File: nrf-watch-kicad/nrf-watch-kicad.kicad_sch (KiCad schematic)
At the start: 78 parts, among them IC1 TLV840MAPL36DBVRQ1, IC2 XC9265C181MR-G, IC3 TPS61023DRLT, IC4 MAX30101EFD+T, M1 Vibrator DC Motor, Q1 DMP2045U-7, Q2 SS8050-G, U1 MAX1811ESA+, U2 DMC2400UV-7, U3 LIS2DS12TR, U4 MX25R6435FZNIL0, U5 u-blox ANNA-B402, U6 DRV2603RUNT, U7 XC9265A331MR-G, U8 TXB0104QRUTRQ1, U9 GC9A01

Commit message: Before moving bottom to top
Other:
- note added: "In case of issues in battery and power management circuit there is a solder bridge that can be unconnected in order for rest of board to still function. If not working I can inject 5V at V_BAT testpoint and at 1.8V regulator CE."
- note added: "Pull-up/down resistors"
- note added: "The 3V3 regulator CE signal will be used as thedisplay reset/on off as nothing else is using 3V3 and I save one level shift for the display RESET signal."
- note removed: "In case of issues in battery and power management circuit there are a solder bridge that can be unconnected in order for rest of board to still function. If not working we can inject 5V at V_BAT testpoint and at 1.8V regulator CE."
- note removed: "Pull-up resistors"
- company: Jakob Krantz -> (none)
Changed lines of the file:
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@@
 (kicad_sch (version 20211123) (generator eeschema)
-  (paper "A2")
+  (paper "User" 419.989 340.004)
   (title_block
     (title "Smart Watch")
     (date "2022-09-05")
     (rev "0.1")
-    (company "Jakob Krantz")
   )
   (junction (at 261.62 55.88) (diameter 0) (color 0 0 0 0)
@@
     (stroke (width 0) (type default) (color 0 0 0 0))
   )
-  (polyline (pts (xy 96.52 152.4) (xy 15.24 152.4))
+  (polyline (pts (xy 73.66 152.4) (xy 15.24 152.4))
     (stroke (width 0) (type default) (color 0 0 0 0))
   )
@@
     (stroke (width 0) (type default) (color 0 0 0 0))
   )
-  (polyline (pts (xy 269.24 281.94) (xy 269.24 121.92))
+  (polyline (pts (xy 271.78 292.1) (xy 269.24 121.92))
     (stroke (width 0) (type default) (color 0 0 0 0))
   )
@@
     (stroke (width 0) (type default) (color 0 0 0 0))
   )
-  (polyline (pts (xy 96.52 121.92) (xy 96.52 152.4))
+  (polyline (pts (xy 73.66 121.92) (xy 73.66 152.4))
     (stroke (width 0) (type default) (color 0 0 0 0))
   )
@@
     (stroke (width 0) (type default) (color 0 0 0 0))
   )
-  (wire (pts (xy 63.5 134.62) (xy 63.5 142.24))
+  (wire (pts (xy 50.8 134.62) (xy 50.8 142.24))
     (stroke (width 0) (type default) (color 0 0 0 0))
   )
@@
     (stroke (width 0) (type default) (color 0 0 0 0))
   )
-  (polyline (pts (xy 172.72 121.92) (xy 172.72 281.94))
+  (polyline (pts (xy 172.72 121.92) (xy 175.26 292.1))
     (stroke (width 0) (type default) (color 0 0 0 0))
   )
@@
     (stroke (width 0) (type default) (color 0 0 0 0))
   )
-  (polyline (pts (xy 172.72 281.94) (xy 269.24 281.94))
+  (polyline (pts (xy 175.26 292.1) (xy 271.78 292.1))
     (stroke (width 0) (type default) (color 0 0 0 0))
   )
@@
     (stroke (width 0) (type default) (color 0 0 0 0))
   )
-  (wire (pts (xy 76.2 134.62) (xy 76.2 139.7))
+  (wire (pts (xy 63.5 134.62) (xy 63.5 139.7))
     (stroke (width 0) (type default) (color 0 0 0 0))
   )
@@
     (stroke (width 0) (type default) (color 0 0 0 0))
   )
-  (polyline (pts (xy 15.24 121.92) (xy 96.52 121.92))
+  (polyline (pts (xy 15.24 121.92) (xy 73.66 121.92))
     (stroke (width 0) (type default) (color 0 0 0 0))
   )
@@
     (effects (font (size 1.27 1.27)) (justify left bottom))
   )
-  (text "Pull-up resistors" (at 109.22 127 0)
+  (text "Pull-up/down resistors" (at 109.22 127 0)
     (effects (font (size 3 3)) (justify left bottom))
   )
@@
     (effects (font (size 1.27 1.27)) (justify left bottom))
   )
-  (text "In case of issues in battery and power management circuit \nthere are a solder bridge that can be unconnected\nin order for rest of board to still function.\n\nIf not working we can inject 5V at V_BAT testpoint and at 1.8V regulator CE."
+  (text "In case of issues in battery and power management circuit \nthere is a solder bridge that can be unconnected\nin order for rest of board to still function.\n\nIf not working I can inject 5V at V_BAT testpoint and at 1.8V regulator CE."
     (at 170.18 30.48 0)
     (effects (font (size 1.27 1.27)) (justify left bottom))
@@
     (effects (font (size 1.27 1.27)) (justify left bottom))
   )
+  (text "The 3V3 regulator CE signal will be used\nas thedisplay reset/on off as nothing\nelse is using 3V3 and I save one level\nshift for the display RESET signal."
+    (at 233.68 279.4 0)
+    (effects (font (size 1.1 1.1)) (justify left bottom))
+  )
   (text "Vibration motor\n(ERM Mode)" (at 281.94 73.66 0)
     (effects (font (size 3 3)) (justify left bottom))
   )
   (text "TODO check so RESET HIGH means ON\nThis signlas will reset the device\nand it must be applied to properly\ninitialize the chip.\nSignal is ACTIVE LOW."
-    (at 233.68 279.4 0)
+    (at 233.68 292.1 0)
     (effects (font (size 1.1 1.1)) (justify left bottom))
   )
@@
     )
   )
-  (global_label "V_BAT" (shape input) (at 63.5 142.24 270) (fields_autoplaced)
+  (global_label "V_BAT" (shape input) (at 50.8 142.24 270) (fields_autoplaced)
     (effects (font (size 1.27 1.27)) (justify right))
-    (property "Intersheet References" "${INTERSHEET_REFS}" (id 0) (at 63.5794 150.0355 90)
+    (property "Intersheet References" "${INTERSHEET_REFS}" (id 0) (at 50.8794 150.0355 90)
       (effects (font (size 1.27 1.27)) (justify right) hide)
     )
@@
     (pin "1")
   )
-  (symbol (lib_id "power:GND") (at 76.2 139.7 0) (unit 1)
+  (symbol (lib_id "power:GND") (at 63.5 139.7 0) (unit 1)
     (in_bom yes) (on_board yes)
-    (property "Reference" "#PWR024" (id 0) (at 76.2 146.05 0)
+    (property "Reference" "#PWR024" (id 0) (at 63.5 146.05 0)
       (effects (font (size 1.27 1.27)) hide)
     )
-    (property "Value" "GND" (id 1) (at 76.2 144.78 0))
-    (property "Footprint" "" (id 2) (at 76.2 139.7 0)
+    (property "Value" "GND" (id 1) (at 63.5 144.78 0))
+    (property "Footprint" "" (id 2) (at 63.5 139.7 0)
       (effects (font (size 1.27 1.27)) hide)
     )
-    (property "Datasheet" "" (id 3) (at 76.2 139.7 0)
+    (property "Datasheet" "" (id 3) (at 63.5 139.7 0)
       (effects (font (size 1.27 1.27)) hide)
     )
@@
     (pin "2")
   )
-  (symbol (lib_id "power:PWR_FLAG") (at 76.2 134.62 0) (unit 1)
+  (symbol (lib_id "power:PWR_FLAG") (at 63.5 134.62 0) (unit 1)
     (in_bom yes) (on_board yes) (fields_autoplaced)
-    (property "Reference" "#FLG05" (id 0) (at 76.2 132.715 0)
+    (property "Reference" "#FLG05" (id 0) (at 63.5 132.715 0)
       (effects (font (size 1.27 1.27)) hide)
     )
-    (property "Value" "PWR_FLAG" (id 1) (at 76.2 130.81 0))
-    (property "Footprint" "" (id 2) (at 76.2 134.62 0)
+    (property "Value" "PWR_FLAG" (id 1) (at 63.5 130.81 0))
+    (property "Footprint" "" (id 2) (at 63.5 134.62 0)
       (effects (font (size 1.27 1.27)) hide)
     )
-    (property "Datasheet" "~" (id 3) (at 76.2 134.62 0)
+    (property "Datasheet" "~" (id 3) (at 63.5 134.62 0)
       (effects (font (size 1.27 1.27)) hide)
     )
@@
     (pin "9")
   )
-  (symbol (lib_id "power:PWR_FLAG") (at 63.5 134.62 0) (unit 1)
+  (symbol (lib_id "power:PWR_FLAG") (at 50.8 134.62 0) (unit 1)
     (in_bom yes) (on_board yes) (fields_autoplaced)
-    (property "Reference" "#FLG04" (id 0) (at 63.5 132.715 0)
+    (property "Reference" "#FLG04" (id 0) (at 50.8 132.715 0)
       (effects (font (size 1.27 1.27)) hide)
     )
-    (property "Value" "PWR_FLAG" (id 1) (at 63.5 130.81 0))
-    (property "Footprint" "" (id 2) (at 63.5 134.62 0)
+    (property "Value" "PWR_FLAG" (id 1) (at 50.8 130.81 0))
+    (property "Footprint" "" (id 2) (at 50.8 134.62 0)
       (effects (font (size 1.27 1.27)) hide)
     )
-    (property "Datasheet" "~" (id 3) (at 63.5 134.62 0)
+    (property "Datasheet" "~" (id 3) (at 50.8 134.62 0)
       (effects (font (size 1.27 1.27)) hide)
     )

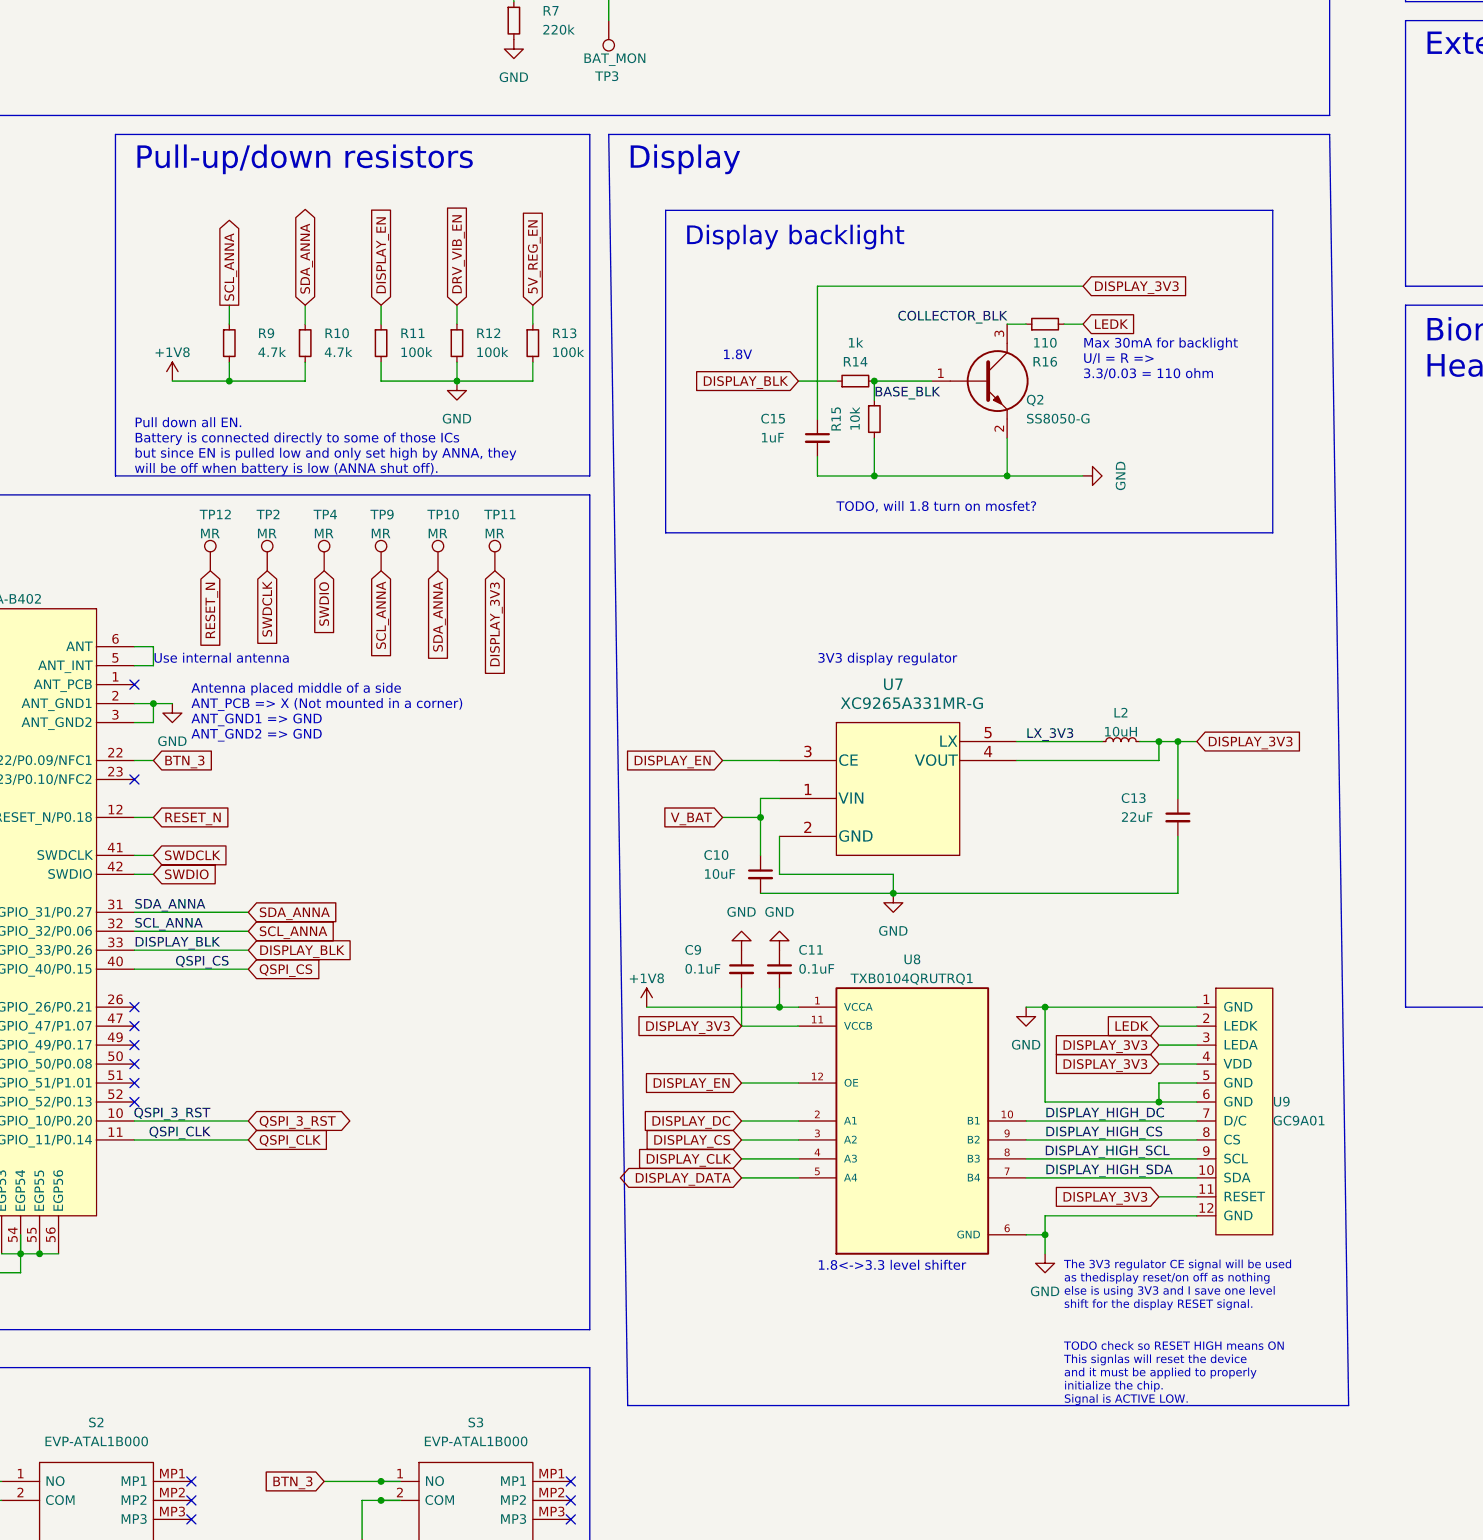
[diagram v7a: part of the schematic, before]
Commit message: Routed out the antenna pins so that a wire antenna could be solder onto it if needed. Added a bunch of test points.
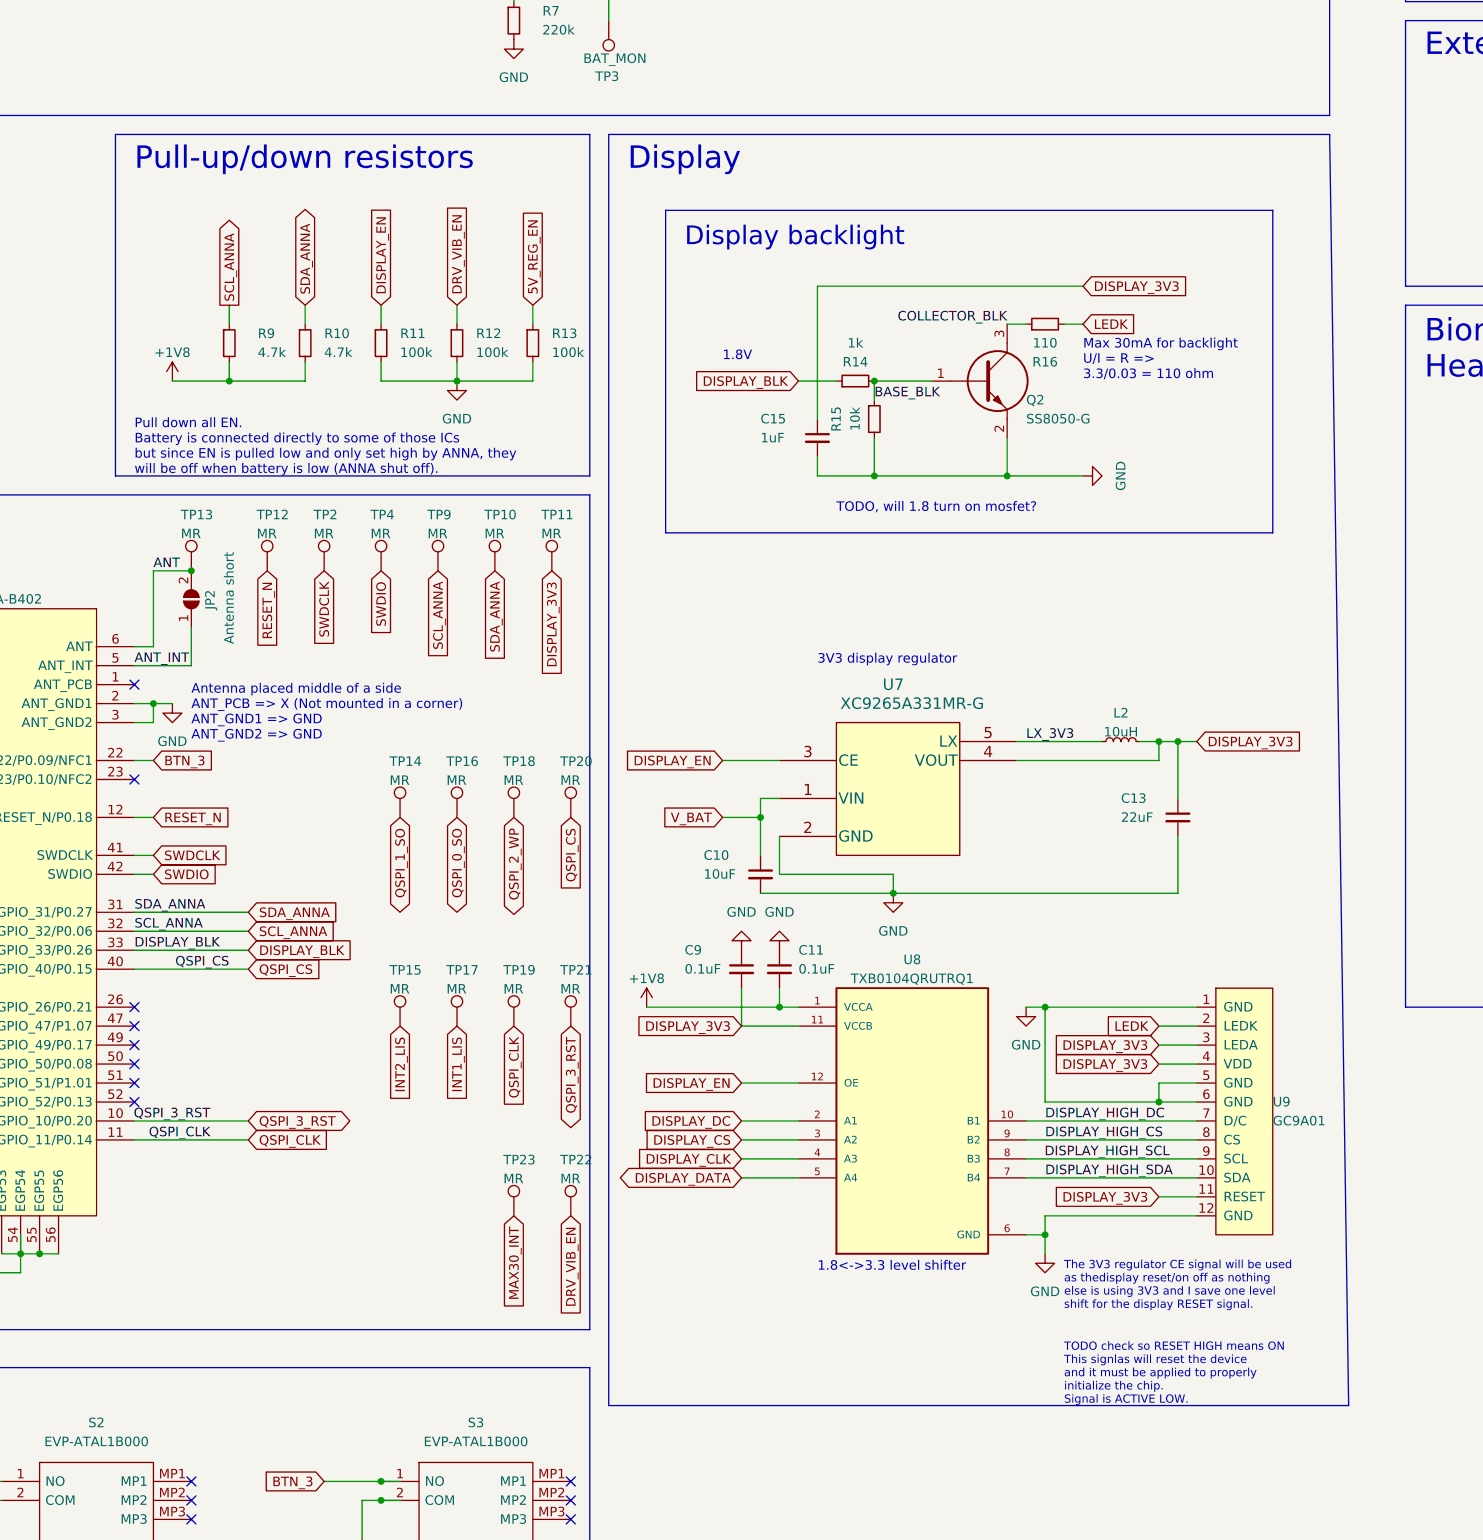
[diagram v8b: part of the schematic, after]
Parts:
- added JP2: Antenna short, Jumper:SolderJumper-2_P1.3mm_Open_Pad1.0x1.5mm, symbol Jumper:SolderJumper_2_Open
- added TP13: MR, TestPoint:TestPoint_Pad_D1.0mm, symbol Connector:TestPoint
- added TP14, TP15, TP16, TP17, TP18, TP19, TP20, TP21, TP22, TP23: MR, user_library:TestPoint_Pad_D0.4mm, symbol Connector:TestPoint
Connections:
- net DRV_VIB_EN: now also TP22.1
- net INT1_LIS: now also TP17.1
- net INT2_LIS: now also TP15.1
- net MAX30_INT: now also TP23.1
- net QSPI_0_SO: now also TP16.1
- net QSPI_1_SO: now also TP14.1
- net QSPI_2_WP: now also TP18.1
- net QSPI_3_RST: now also TP21.1
- net QSPI_CLK: now also TP19.1
- net QSPI_CS: now also TP20.1
- net ANT: now reaches U5.6 (ANT)
- net ANT: now also JP2.2 (B), TP13.1; no longer U5.5 (ANT_INT)
- new net ANT_INT: JP2.1 (A), U5.5 (ANT_INT)
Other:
- note removed: "Use internal antenna"
- moved on the sheet: TP10, TP11, TP12, TP2, TP4, TP9
